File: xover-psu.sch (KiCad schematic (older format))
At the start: 103 parts, among them J1 Screw_Terminal_01x03, J2 Screw_Terminal_01x02, J3 Screw_Terminal_01x02, J4 Screw_Terminal_01x03, J5 Screw_Terminal_01x03, J6 Screw_Terminal_01x02, J7 Screw_Terminal_01x02, J8 Screw_Terminal_01x03, K2 T9GS1L14-12, Q1 AO3400, Q2 2N7002, Q3 AO3400, U1 817C, U2 TL431DBZ, U4 LM317_3PinPackage, U5 LM337_TO220, U6 TL431DBZ, U8 817C

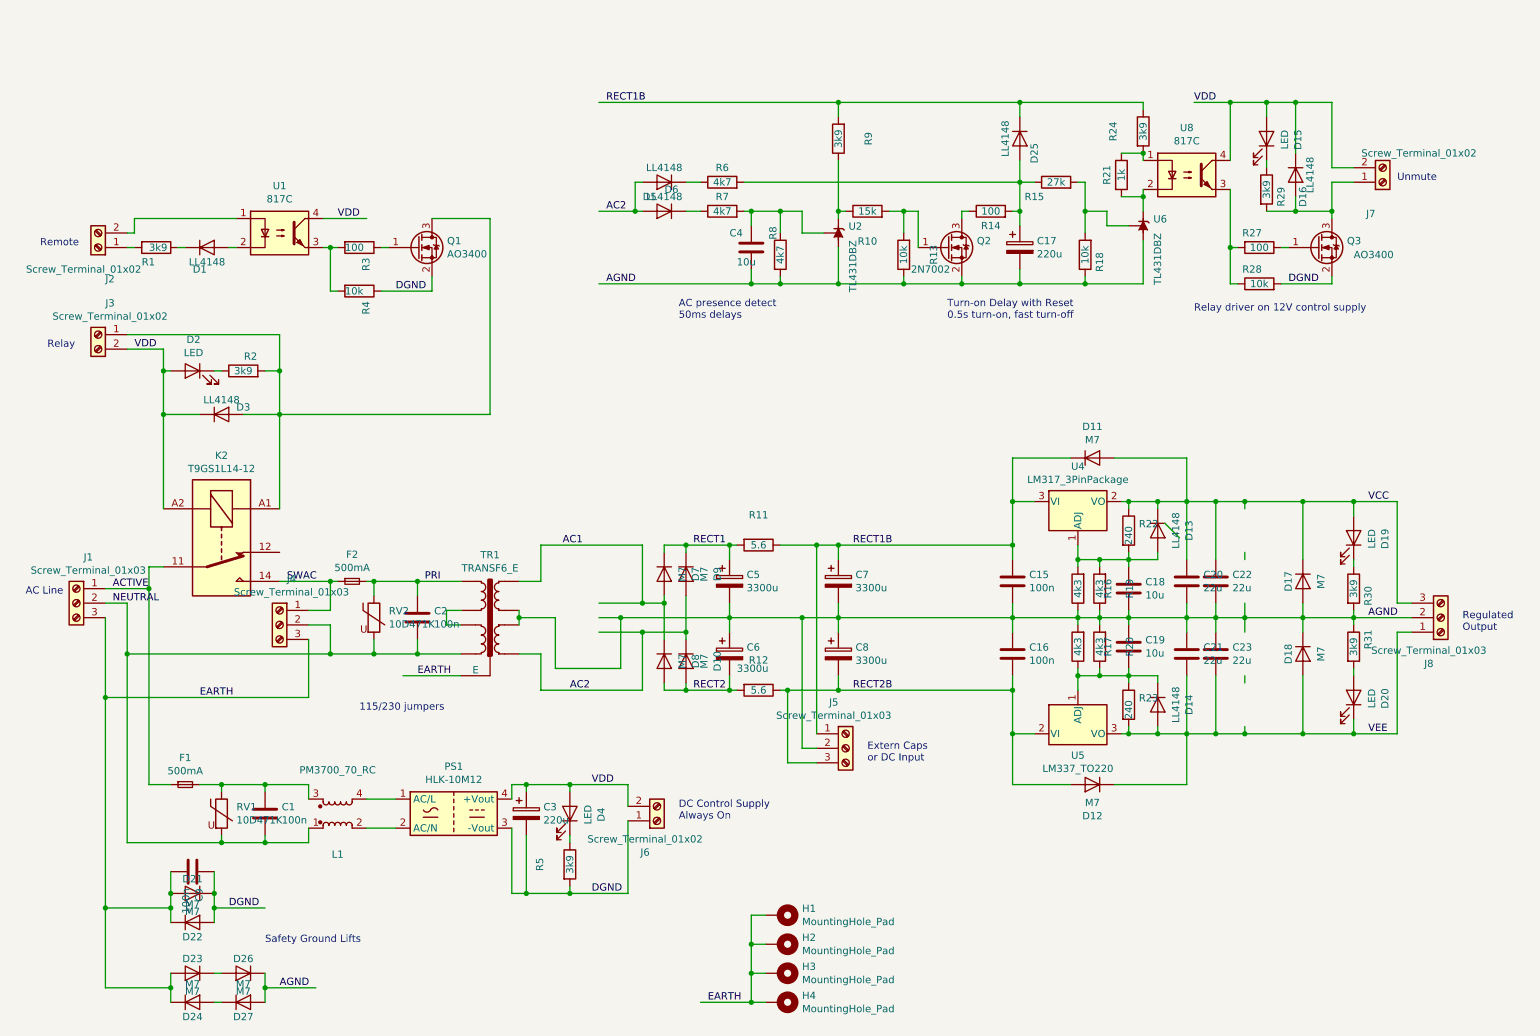
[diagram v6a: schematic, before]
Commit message: updated schematic for faster turn-on transition for UNMUTE
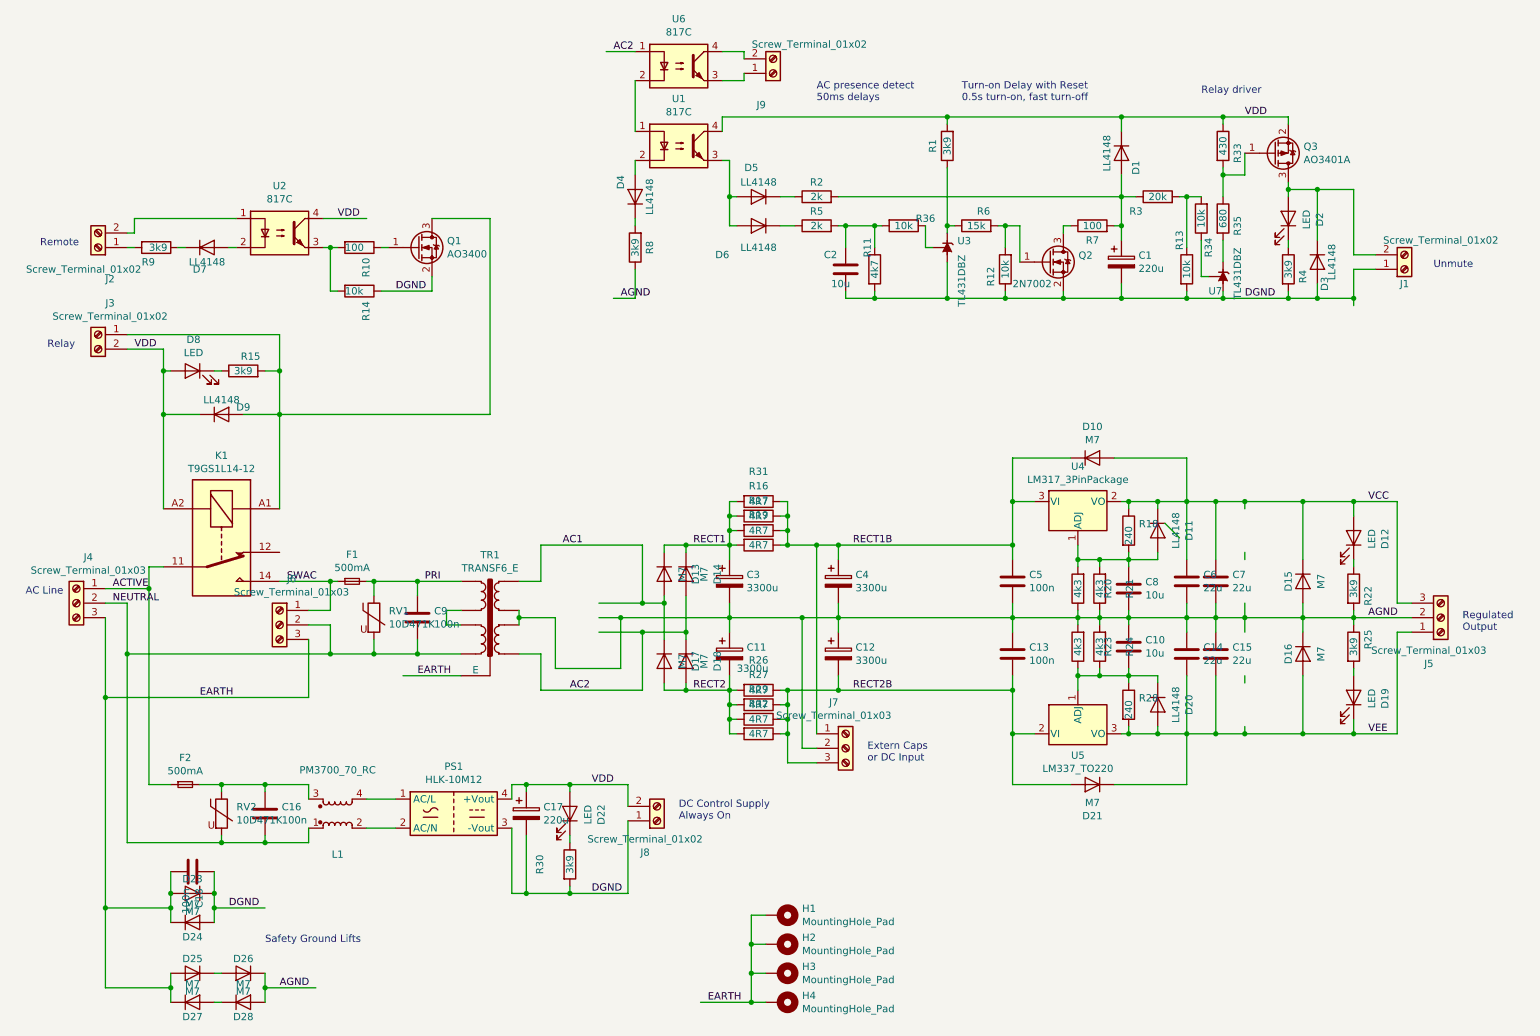
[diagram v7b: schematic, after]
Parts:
- removed C17: 220u, Capacitors_SMD:CP_Elec_10x10, symbol Device:CP
- removed C4: 10u, Capacitors_SMD:C_1210, symbol Device:C
- removed D15: LED, LEDs:LED_0805, symbol Device:LED
- removed D16, D25: LL4148, Diodes_SMD:D_MiniMELF, symbol Device:D
- removed J7: Screw_Terminal_01x02, Terminals_Phoenix:TerminalBlock_Phoenix_MKDS1.5-2pol, symbol Connector:Screw_Terminal_01x02
- removed Q3: AO3400, TO_SOT_Packages_SMD:SOT-23, symbol Device:Q_NMOS_GSD
- removed R10: 15k, Resistors_SMD:R_0805, symbol Device:R
- removed R14: 100, Resistors_SMD:R_0805, symbol Device:R
- removed R15: 27k, Resistors_SMD:R_0805, symbol Device:R
- removed R18, R28: 10k, Resistors_SMD:R_0805, symbol Device:R
- removed R21: 1k, Resistors_SMD:R_0805, symbol Device:R
- removed R24, R9: 3k9, Resistors_SMD:R_0805, symbol Device:R
- removed U2, U6: TL431DBZ, TO_SOT_Packages_SMD:SOT-23, symbol Reference_Voltage:TL431DBZ
- removed U8: 817C, Housings_DIP:DIP-4_W7.62mm_Socket, symbol Isolator:PC817
- added C1: 220u, Capacitors_SMD:CP_Elec_10x10, symbol Device:CP
- added C2: 10u, Capacitors_SMD:C_1210, symbol Device:C
- added D1, D3, D4: LL4148, Diodes_SMD:D_MiniMELF, symbol Device:D
- added D2: LED, LEDs:LED_0805, symbol Device:LED
- added J1, J9: Screw_Terminal_01x02, Terminals_Phoenix:TerminalBlock_Phoenix_MKDS1.5-2pol, symbol Connector:Screw_Terminal_01x02
- added Q3: AO3401A, TO_SOT_Packages_SMD:SOT-23, symbol Transistor_FET:AO3401A
- added R1, R4: 3k9, Resistors_SMD:R_0805, symbol Device:R
- added R11: 4k7, Resistors_SMD:R_0805, symbol Device:R
- added R16, R17, R26, R31, R32: 4R7, Resistors_SMD:R_0805, symbol Device:R
- added R2, R5: 2k, Resistors_SMD:R_0805, symbol Device:R
- added R3: 20k, Resistors_SMD:R_0805, symbol Device:R
- added R33: 430, Resistors_SMD:R_0805, symbol Device:R
- added R34, R36: 10k, Resistors_SMD:R_0805, symbol Device:R
- added R35: 680, Resistors_SMD:R_0805, symbol Device:R
- added U1, U6: 817C, Housings_DIP:DIP-4_W7.62mm_Socket, symbol Isolator:PC817
- added U3, U7: TL431DBZ, TO_SOT_Packages_SMD:SOT-23, symbol Reference_Voltage:TL431DBZ
- R12: value 5.6 -> 10k; footprint Resistors_ThroughHole:R_Axial_DIN0414_L11.9mm_D4.5mm_P5.08mm_Vertical -> Resistors_SMD:R_0805
- R19: renamed from R11; value 5.6 -> 4R7; footprint Resistors_ThroughHole:R_Axial_DIN0414_L11.9mm_D4.5mm_P5.08mm_Vertical -> Resistors_SMD:R_0805
- R27: value 100 -> 4R7
- R29: value 3k9 -> 4R7
- R6: value 4k7 -> 15k
- R7: value 4k7 -> 100
- R8: value 4k7 -> 3k9
- renumbered C19 to C10, C6 to C11, C8 to C12, C16 to C13, C21 to C14, C23 to C15, C1 to C16, C3 to C17, C9 to C18, C5 to C3, C7 to C4, C15 to C5, C20 to C6, C22 to C7, C18 to C8, C2 to C9, D11 to D10, D13 to D11, D19 to D12, D7 to D13, D9 to D14, D17 to D15, D18 to D16, D8 to D17, D10 to D18, D20 to D19, D14 to D20, D12 to D21, D4 to D22, D21 to D23, D22 to D24, D23 to D25, D24 to D27, D27 to D28, D1 to D7, D2 to D8, D3 to D9, F2 to F1, F1 to F2, J1 to J4, J8 to J5, J4 to J6, J5 to J7, J6 to J8, K2 to K1, R3 to R10, R4 to R14, R2 to R15, R22 to R18, R16 to R20, R19 to R21, R30 to R22, R17 to R23, R20 to R24, R31 to R25, R23 to R28, R5 to R30, R1 to R9, RV2 to RV1, RV1 to RV2, U1 to U2
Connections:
- wire segments 354 -> 384
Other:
- note added: "Relay driver"
- note removed: "115/230 jumpers"
- note removed: "Relay driver on 12V control supply"

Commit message: tested UNMUTE circuit, improved switch-on/off speed, rejigged mains routing for EMI
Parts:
- C15, C7: symbol Device:C -> Device:CP
- K1: value T9GS1L14-12 -> T9GS1L24-12
- R18, R28: value 240 -> 270
- R20, R23: value 4k3 -> 5k1
- R21, R24: value 4k3 -> 6k8
- R35: value 680 -> 1k
- U1, U2, U6: footprint Housings_DIP:DIP-4_W7.62mm_Socket -> Housings_DIP:DIP-4_W7.62mm
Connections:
- wire segments 384 -> 364
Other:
- note added: "AC Pulses"
- moved on the sheet: C12, C4, J7
